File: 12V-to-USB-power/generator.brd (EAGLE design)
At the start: 93.7 x 69.8 mm, 62 parts, among them IC1 MC34063AD, K1 ARK500/2, K2 ARK500/2, K3 ARK500/2, K4 ARK500/2, K5 ARK500/2, K6 HEAT_NPN, K7 ARK500/2, K8 ARK500/2, Q1 IRF3704S, Q2 IRF3704S, T1 BC807, T2 BC807, X1 CV_LED, X2 PWR_LED, X3 5V_SW, X4 5V_LED, X5 5V_OUT

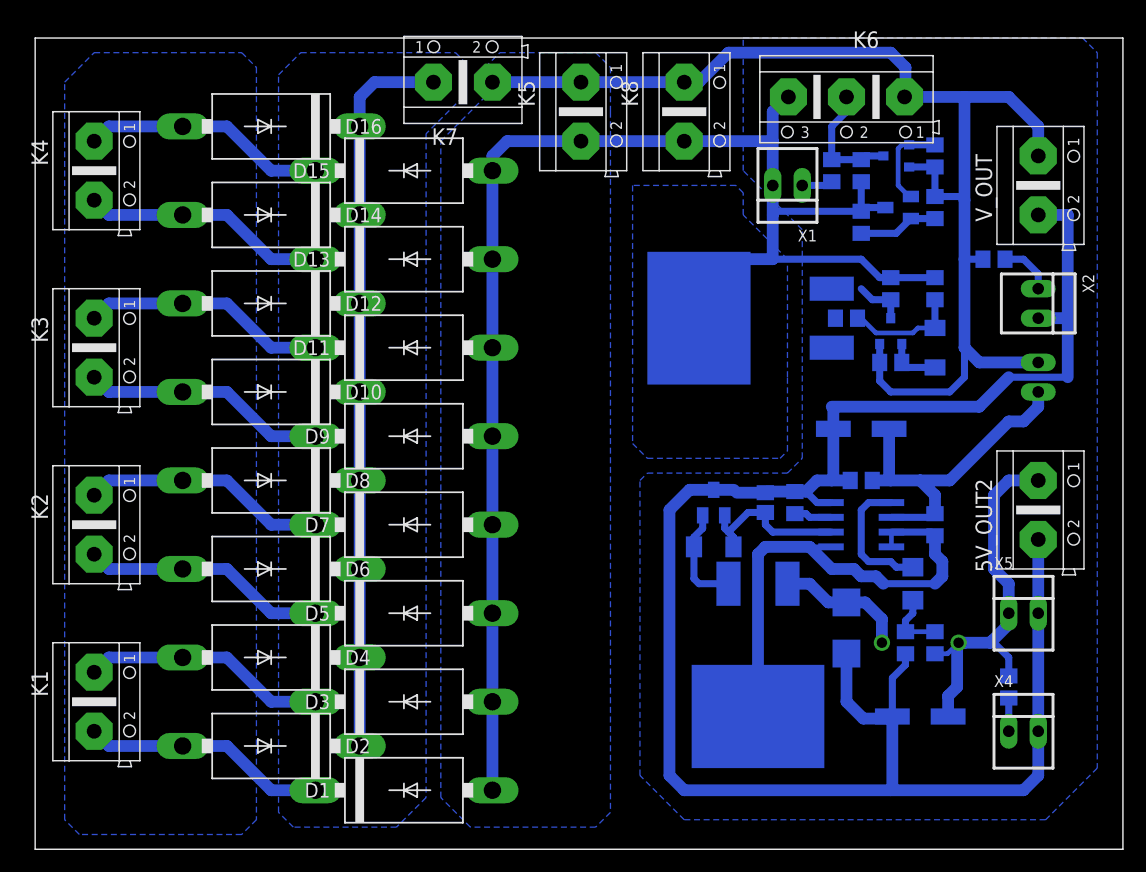
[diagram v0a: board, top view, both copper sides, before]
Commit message: Added 12V to 5V switching regulator with MC34063 and MOSFET.
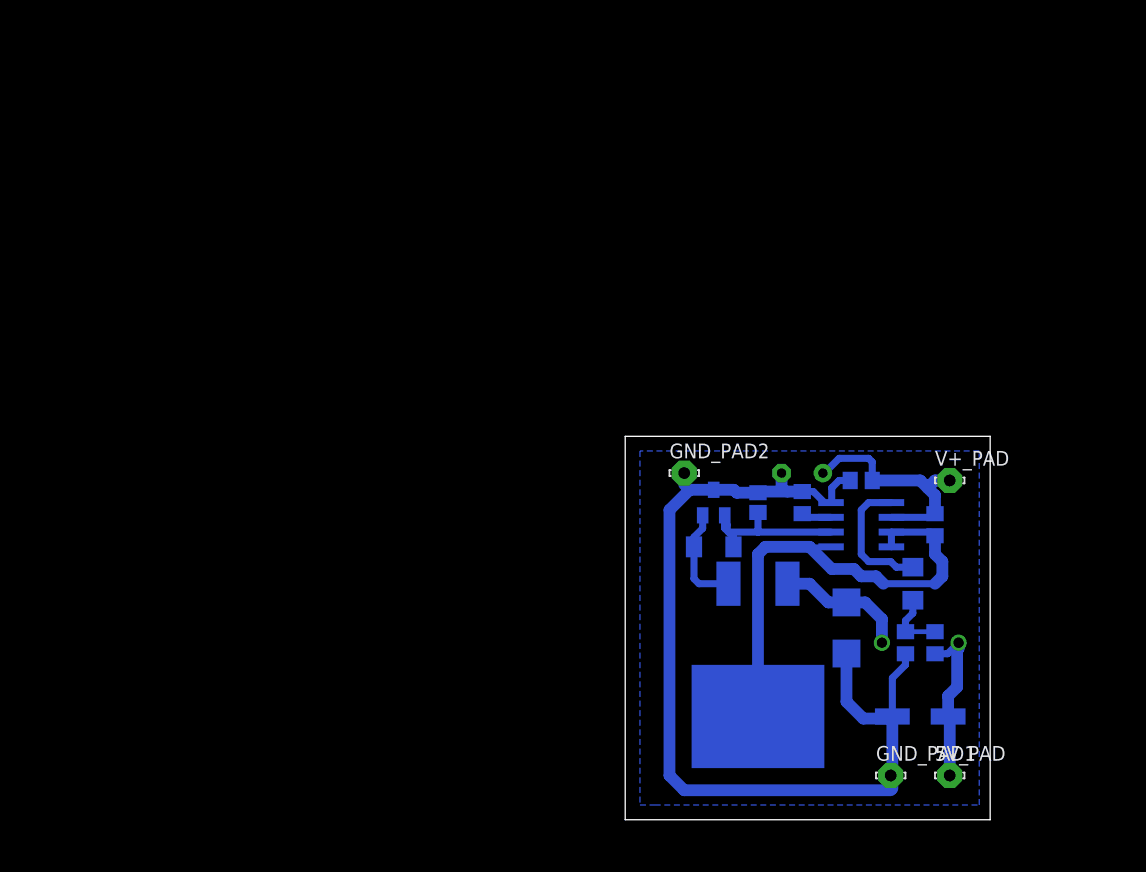
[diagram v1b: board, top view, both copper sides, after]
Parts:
- removed 5V_OUT2, K1, K2, K3, K4, K5, K7, K8, V_OUT: ARK500/2, #PaJa_konektory:ARK500/2
- removed D1, D10, D11, D12, D13, D14, D15, D16, D2, D3, D4, D5, D6, D7, D8, D9: 1N5400, diode:DO201-15
- removed D17: 6V2, diode:SOD80C
- removed IO1: TL431SOT23, references:SOT23
- removed K6: HEAT_NPN, #PaJa_konektory:ARK500/3
- removed Q1: IRF3704S, transistor-power:D2PACK
- removed R1, R3, R8: 10k, rcl:R0805
- removed R10, R2, R6, R7, R9: 1k, rcl:R0805
- removed R14: 330, rcl:R0805
- removed R4: 56k, rcl:R0805
- removed R5: 15k, rcl:R0805
- removed T1, T2: BC807, #PaJa_30:SOT-23
- removed X1: CV_LED, con-molex:22-23-2021
- removed X2: PWR_LED, con-molex:22-23-2021
- removed X3: 5V_SW, con-molex:22-23-2021
- removed X4: 5V_LED, con-molex:22-23-2021
- removed X5: 5V_OUT, con-molex:22-23-2021
- added 5V_PAD, GND_PAD1, GND_PAD2, V+_PAD: LSP10, solpad:LSP10
- C4: device rcl:PANASONIC_D -> rcl:E3,5-10
- moved C4 6.35 mm to (66.0, 42.5), turned to 0 degrees
- moved C1 0.64 mm to (66.0, 40.0)
- moved R18 0.64 mm to (62.2, 40.0)
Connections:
- removed net N$1: D1.A, D2.C, K1.2
- removed net N$10: D11.A, D12.C, K3.1
- removed net N$12: IO1.2, R5.1, R6.2
- removed net N$13: D13.A, D14.C, K4.2
- removed net N$14: D15.A, D16.C, K4.1
- removed net N$17: D17.C, R1.1, T1.1
- removed net N$18: D17.A, R2.2, R3.2
- removed net N$2: D3.A, D4.C, K1.1
- removed net N$20: D1.C, D11.C, D13.C, D15.C, D3.C, D5.C, D7.C, D9.C, K7.1
- removed net N$22: R14.1, X4.1
- removed net N$23: R10.1, X2.1
- removed net N$24: C2.1, C4.+, IC1.6, R13.1, X3.2
- removed net N$3: IO1.1, R7.1, T2.1
- removed net N$4: Q1.1, R4.1, T1.3
- removed net N$5: D5.A, D6.C, K2.2
- removed net N$6: D7.A, D8.C, K2.1
- removed net N$7: K6.2, R8.2, R9.2, T2.3
- removed net N$8: R9.1, X1.1
- removed net N$9: D10.C, D9.A, K3.2
- removed net V-: D10.A, D12.A, D14.A, D16.A, D2.A, D4.A, D6.A, D8.A, IO1.3, K5.2, K6.3, K8.2, Q1.3, R2.1, R4.2, R6.1, R8.1, X1.2
- net +5V: now also 5V_PAD.MP; no longer 5V_OUT2.1, R14.2, X5.1
- net GND: now also GND_PAD1.MP, GND_PAD2.MP; no longer 5V_OUT2.2, Q1.2, R3.1, V_OUT.2, X2.2, X4.2, X5.2
- net V+: now also C2.1, C4.+, IC1.6, R13.1, V+_PAD.MP; no longer K5.1, K6.1, K7.2, K8.1, R1.2, R10.2, R5.2, R7.2, T1.2, T2.2, V_OUT.1, X3.1
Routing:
- net V-: track 130.2 -> 0.00 mm
- net V+: track 107.5 -> 20.2 mm
- net GND: track 165.0 -> 85.2 mm
- net N$20: track 62.8 -> 0.00 mm
- net N$24: track 30.0 -> 0.00 mm
- net N$2: track 21.2 -> 0.00 mm
- net N$13: track 21.2 -> 0.00 mm
- net N$9: track 21.2 -> 0.00 mm
- net N$5: track 21.2 -> 0.00 mm
- net N$14: track 21.2 -> 0.00 mm
- net N$1: track 21.2 -> 0.00 mm
- net N$6: track 21.2 -> 0.00 mm
- net N$10: track 21.2 -> 0.00 mm
- net +5V: track 33.9 -> 14.3 mm
- net N$7: track 10.5 -> 0.00 mm
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- removed copper zone on layer 16, net N$20
- removed copper zone on layer 16, net N$25
- removed copper zone on layer 16, net V-
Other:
- board size 93.7 x 69.8 mm -> 31.4 x 33 mm
